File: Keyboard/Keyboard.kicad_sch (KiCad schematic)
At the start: 205 parts, among them J1 USB_C_Receptacle_USB2.0_14P, J2 Conn_01x03, J3 Conn_01x03, J4 Conn_01x04, SW1 SW_Push, SW10 SW_Push, SW11 SW_Push, SW12 SW_Push, SW13 SW_Push, SW14 SW_Push, SW15 SW_Push, SW16 SW_Push, SW17 SW_Push, SW18 SW_Push, SW19 SW_Push, SW2 SW_Push, SW20 SW_Push, SW21 SW_Push, SW22 SW_Push, SW23 SW_Push, SW24 SW_Push, SW25 SW_Push, SW26 SW_Push, SW27 SW_Push, SW28 SW_Push, SW29 SW_Push, SW3 SW_Push, SW30 SW_Push, SW31 SW_Push, SW32 SW_Push, SW33 SW_Push, SW34 SW_Push, SW35 SW_Push, SW36 SW_Push, SW37 SW_Push, SW38 SW_Push, SW39 SW_Push, SW4 SW_Push, SW40 SW_Push, SW41 SW_Push, SW42 SW_Push, SW43 SW_Push, SW44 SW_Push, SW45 SW_Push, SW46 SW_Push, SW47 SW_Push, SW48 SW_Push, SW49 SW_Push, SW5 SW_Push, SW50 SW_Push, SW51 SW_Push, SW52 SW_Push, SW53 SW_Push, SW54 SW_Push, SW55 SW_Push, SW56 SW_Push, SW57 SW_Push, SW58 SW_Push, SW59 SW_Push, SW6 SW_Push, SW60 SW_Push, SW61 SW_Push, SW62 SW_Push, SW63 SW_Push, SW64 SW_Push, SW65 SW_Push, SW66 SW_Push, SW67 SW_Push, SW68 SW_Push, SW69 SW_Push, SW7 SW_Push, SW70 SW_Push, SW71 SW_Push, SW72 SW_Push, SW73 SW_Push, SW74 SW_Push, SW75 SW_Push, SW76 SW_Push, SW77 RotaryEncoder_Switch, SW8 SW_Push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

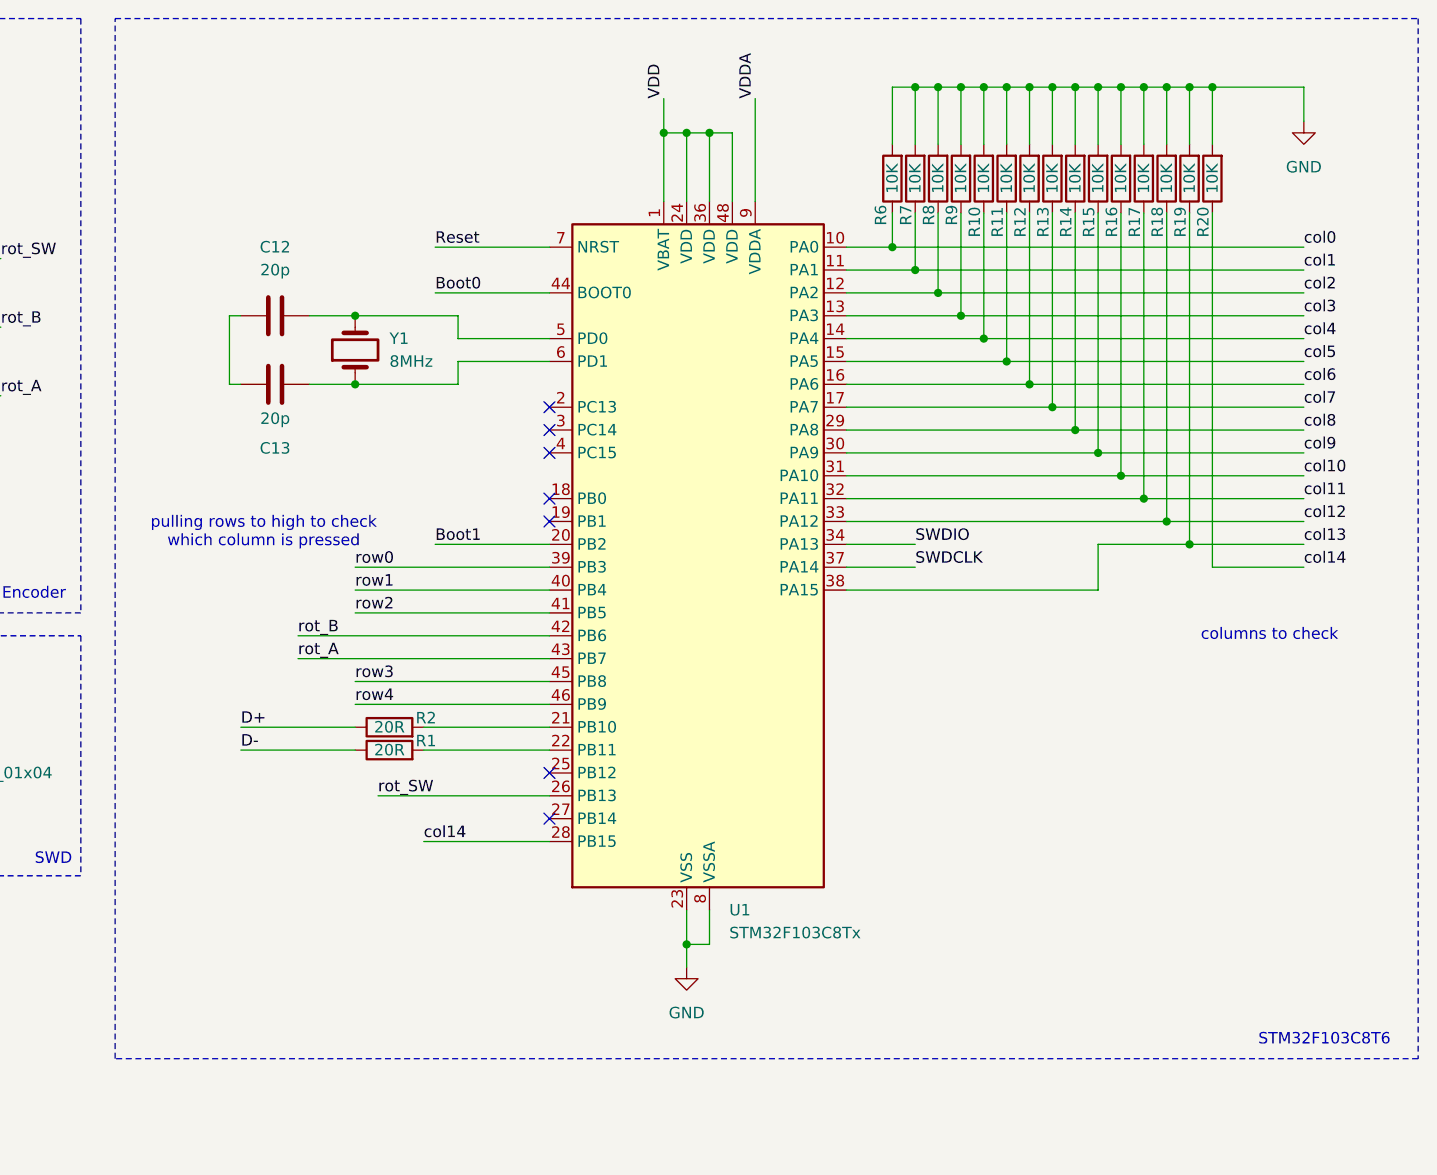
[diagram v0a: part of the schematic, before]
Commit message: Update schematic
add groudn to load capacitors, 1M parallel to oscillator. Fixed connection to D+/D-. Hardware Layout still pending.
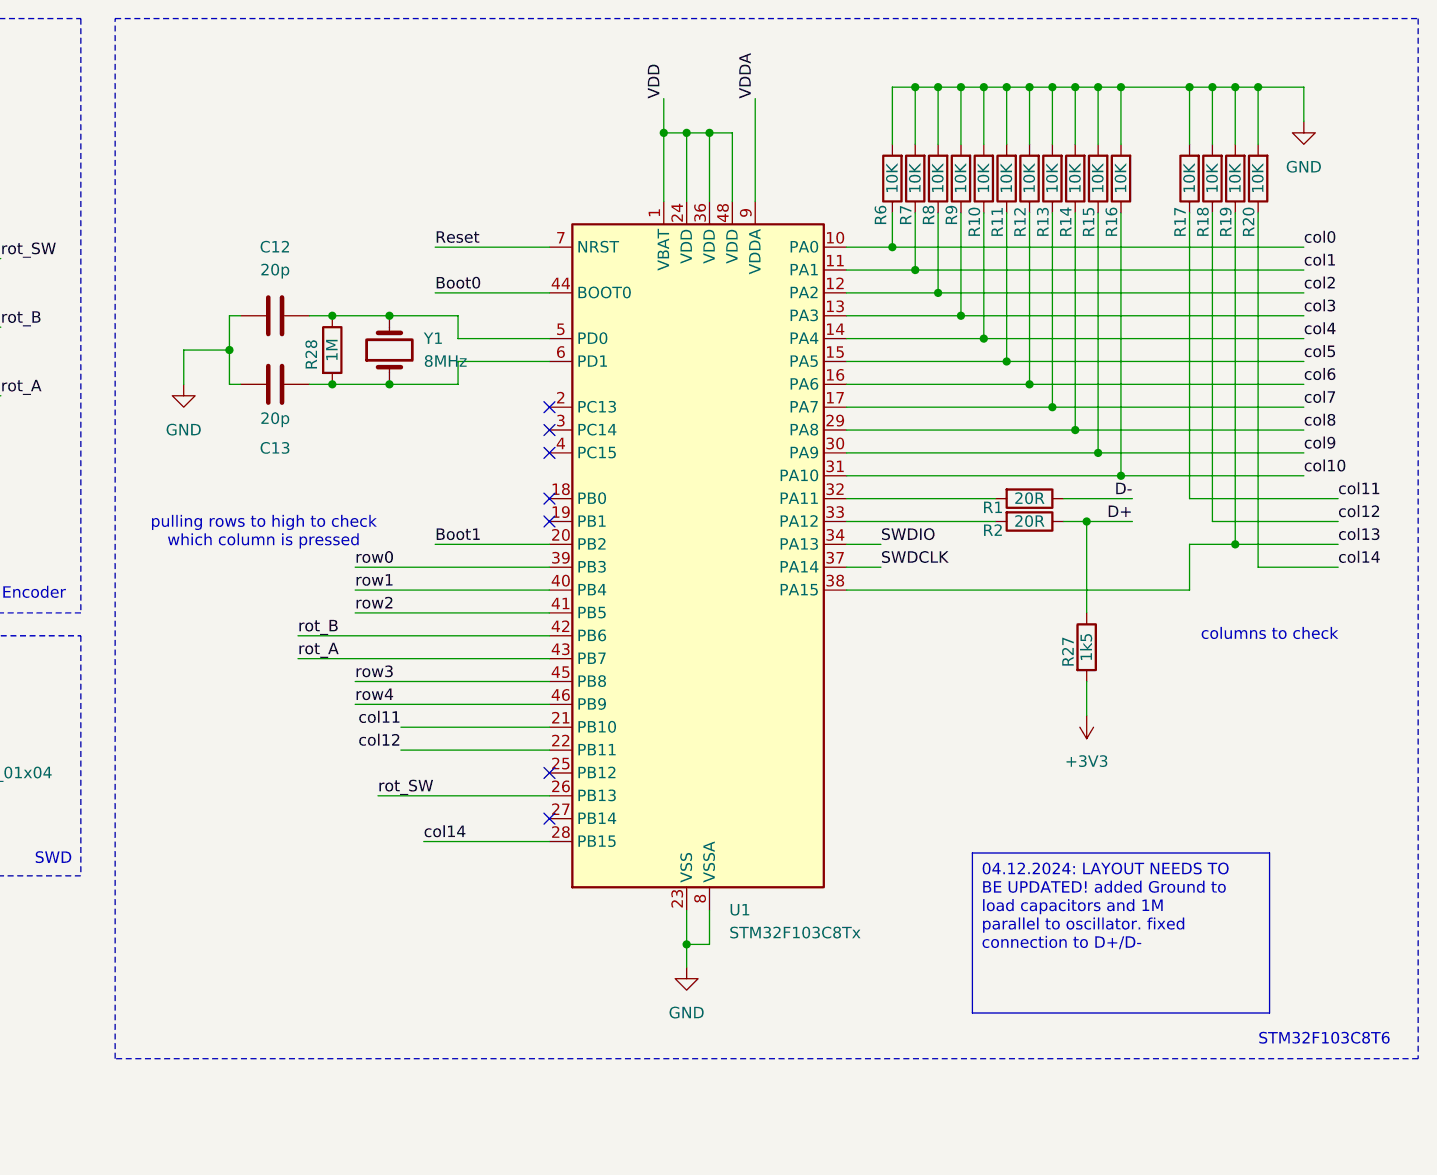
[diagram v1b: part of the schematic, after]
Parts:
- added R27: 1k5, Resistor_SMD:R_0603_1608Metric, symbol Device:R
- added R28: 1M, Resistor_SMD:R_0603_1608Metric, symbol Device:R
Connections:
- net +3V3: now also R27.2
- net D+: now also R27.1
- net GND: now also C12.1, C13.2
- net col11: now also U1.21 (PB10); no longer U1.32 (PA11)
- net col12: now also U1.22 (PB11); no longer U1.33 (PA12)
- net at R2.2: now also U1.33 (PA12); no longer U1.21 (PB10)
- net at R1.2: now also U1.32 (PA11); no longer U1.22 (PB11)
- net at C12.2, U1.5 (PD0), Y1.2: now also R28.1
- net at C13.1, U1.6 (PD1), Y1.1: now also R28.2
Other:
- moved on the sheet: R1, R17, R18, R19, R2, R20, Y1
